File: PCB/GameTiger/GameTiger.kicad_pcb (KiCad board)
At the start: 2 copper layers, 86.4 x 107.2 mm, 73 parts, among them J1 USB_C_Receptacle_USB2.0, J2 503398-1892, J3 LCD Display, J4 Speaker, Q1 DMG3415, U1 RP2040, U2 MCP73831-2-OT, U3 W25Q128JVSIQ, U4 PAM8302A, U5 AP2112K-3.3, U6 PCF8574TS, Y1 ABLS-12MHZ-B4-T

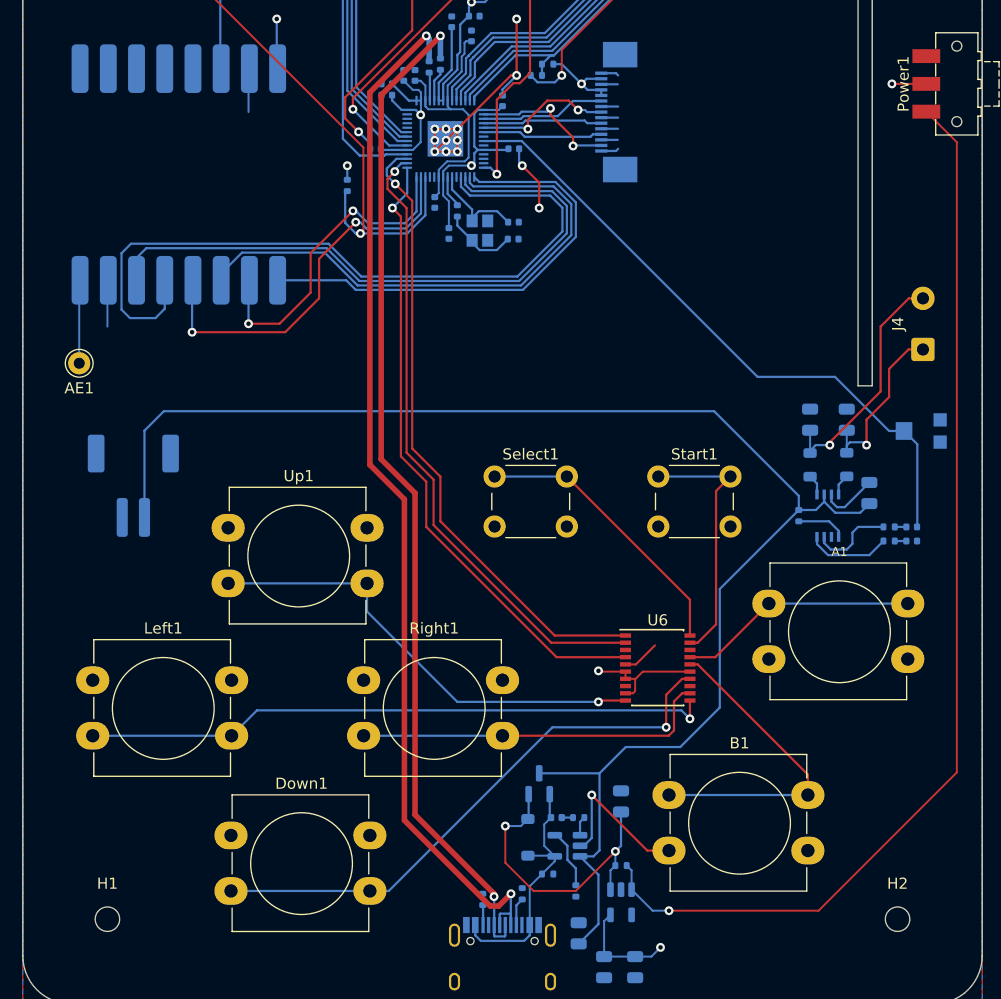
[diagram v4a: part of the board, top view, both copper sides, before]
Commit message: PCB layout and component reference completed
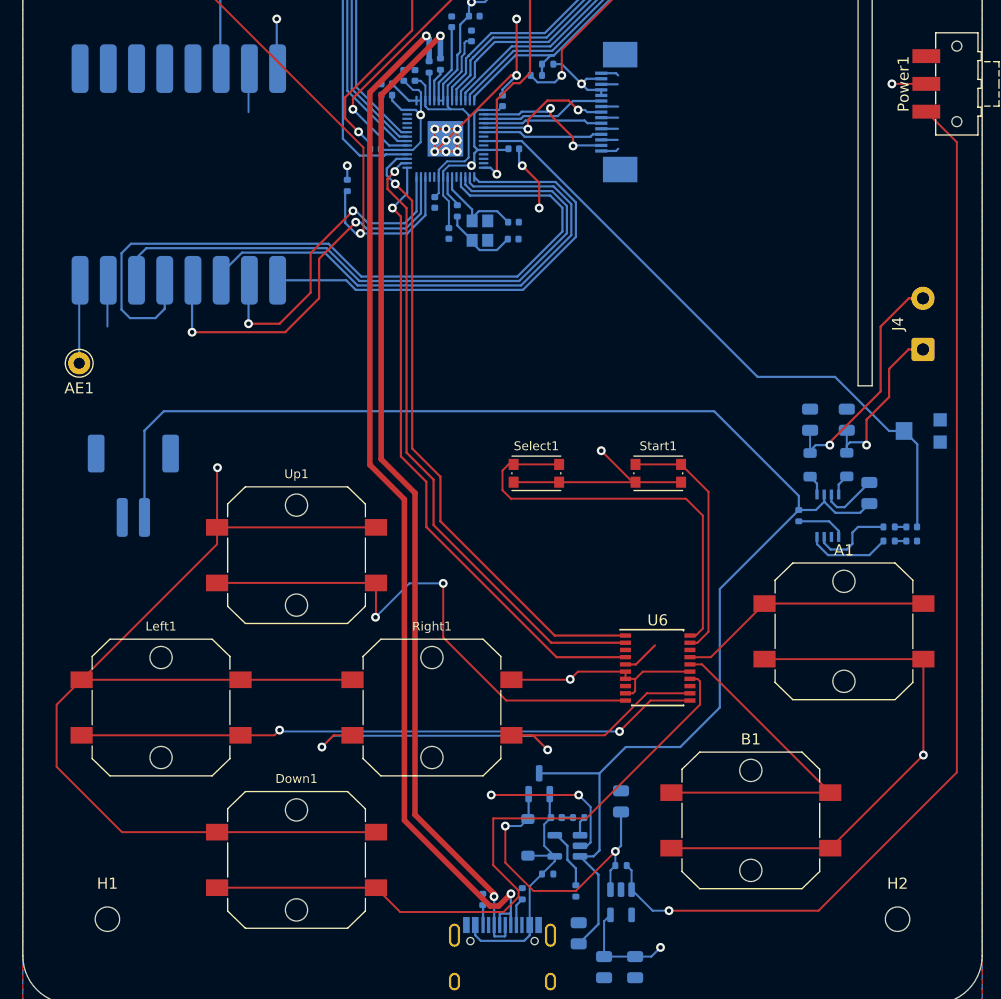
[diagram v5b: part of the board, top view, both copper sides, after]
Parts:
- A1, B1, Down1, Left1, Right1, Up1: footprint Button_Switch_THT:SW_PUSH-12mm_Wuerth-430476085716 -> Button_Switch_SMD:SW_Push_1P1T_NO_CK_PTS125Sx43PSMTR
- Select1, Start1: footprint Button_Switch_THT:SW_PUSH_6mm -> Button_Switch_SMD:SW_Push_1P1T_NO_CK_KMR2
- moved B1 7.71 mm to (98.6, 120.7)
- moved A1 7.21 mm to (106.9, 103.6)
- moved Up1 6.62 mm to (57.7, 96.8)
- moved Left1 6.62 mm to (45.5, 110.5)
- moved Right1 6.62 mm to (69.8, 110.5)
- moved Down1 6.30 mm to (57.7, 124.2)
- moved Select1 3.77 mm to (79.2, 89.4)
- moved Start1 0.29 mm to (90.2, 89.4)
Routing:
- net GND: track 153.3 -> 331.0 mm, vias 21 -> 25
- net KYBD_RIGHT: track 32.5 -> 45.9 mm, vias 0 -> 2
- net KYBD_SELECT: track 25.4 -> 37.7 mm
- net KYBD_DOWN: track 50.9 -> 62.6 mm, vias 1 -> 0
- net KYBD_UP: track 41.7 -> 48.4 mm, vias 1 -> 2
- net KYBD_B: track 29.1 -> 31.7 mm
- net SX1262_CS: track 57.2 -> 55.2 mm
- net KYBD_A: track 21.6 -> 23.0 mm
- net KYBD_START: track 23.4 -> 22.3 mm
- net SX1262_MISO: track 49.3 -> 48.6 mm
- net KYBD_LEFT: track 56.7 -> 56.2 mm, vias 1 -> 2

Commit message: Ready for uploading to JLCPCB
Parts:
- Power1: moved to B.Cu
- R1, R5: value 1kΩ -> 1k
- R10, R12, R13, R16, R6, R7: value 10KΩ -> 10K
- R11, R14, R15: value 5.1KΩ -> 5.1K
- R2: value 10kΩ -> 10K
- R3, R4: value 27Ω -> 27; footprint Resistor_SMD:R_0402_1005Metric -> Resistor_SMD:R_0603_1608Metric
- R8, R9: value 100Ω -> 100
- U6: footprint Package_SO:SSOP-20_4.4x6.5mm_P0.65mm -> PCF8574TS:SOP65P640X150-20N; moved to B.Cu
- moved AE1 29.2 mm to (38.1, 50.3)
- moved C15 6.72 mm to (72.4, 55.4)
- moved J2 5.79 mm to (74.7, 43.7), turned to -90 degrees
- moved Reset1 5.73 mm to (47.8, 38.1)
- moved Boot1 5.48 mm to (104.4, 38.1)
- moved C16 4.71 mm to (74.5, 52.9)
- moved C3 4.39 mm to (77.2, 72.7)
- moved Y1 4.39 mm to (74.2, 72.0)
- moved C8 4.39 mm to (77.2, 64.6)
- moved U3 4.39 mm to (91.4, 40.8)
- moved C12 4.39 mm to (65.8, 58.8)
- moved C13 4.39 mm to (70.1, 69.4)
- moved C14 4.39 mm to (76.2, 60.3)
- moved C2 4.39 mm to (77.2, 71.2)
- moved C5 4.39 mm to (65.8, 59.8)
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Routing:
- net GND: track 331.0 -> 276.0 mm, vias 25 -> 24
- net KYBD_UP: track 48.4 -> 79.0 mm, vias 2 -> 1
- net SX1262_DIO1: track 71.4 -> 49.4 mm
- net Net-(AE1-A): track 7.39 -> 28.7 mm
- net KYBD_A: track 23.0 -> 38.9 mm, vias 0 -> 1
- net MicroSD_CLK: track 29.0 -> 41.3 mm, vias 2 -> 0
- net MicroSD_DETECT: track 43.6 -> 52.8 mm
- net +3.3V: track 87.2 -> 79.7 mm, vias 8 -> 10
- net POWER_USB_DM: track 95.4 -> 88.7 mm
- net KYBD_SELECT: track 37.7 -> 31.3 mm, vias 0 -> 1
- net KYBD_LEFT: track 56.2 -> 50.3 mm, vias 2 -> 1
- net Net-(U1-RUN): track 57.9 -> 63.0 mm
- net MicroSD_MISO: track 38.5 -> 34.0 mm, vias 0 -> 2
- net KYBD_DOWN: track 62.6 -> 66.8 mm, vias 0 -> 1
- net POWER_USB_DP: track 91.5 -> 87.9 mm
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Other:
- board size 86.4 x 107.2 mm -> 86.4 x 99.8 mm

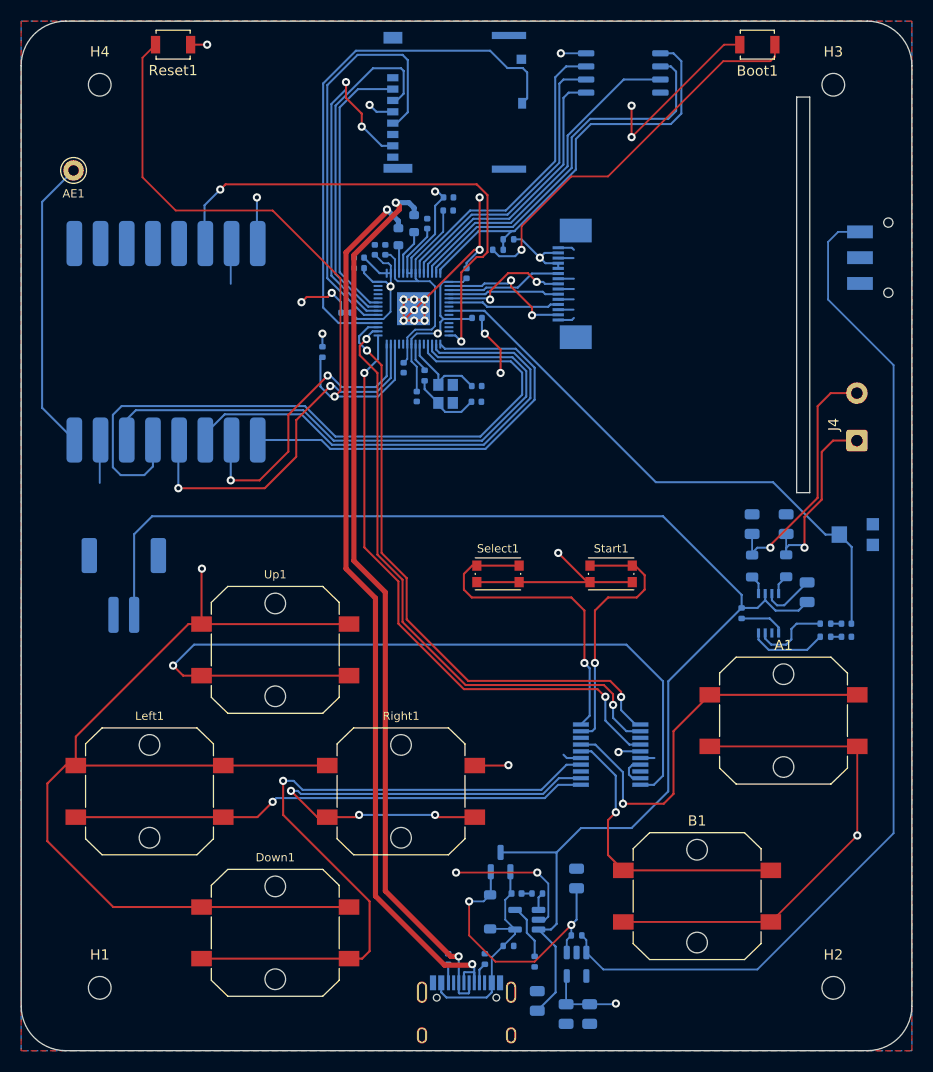
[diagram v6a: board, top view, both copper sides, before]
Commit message: Added battery level and charge detect connectors
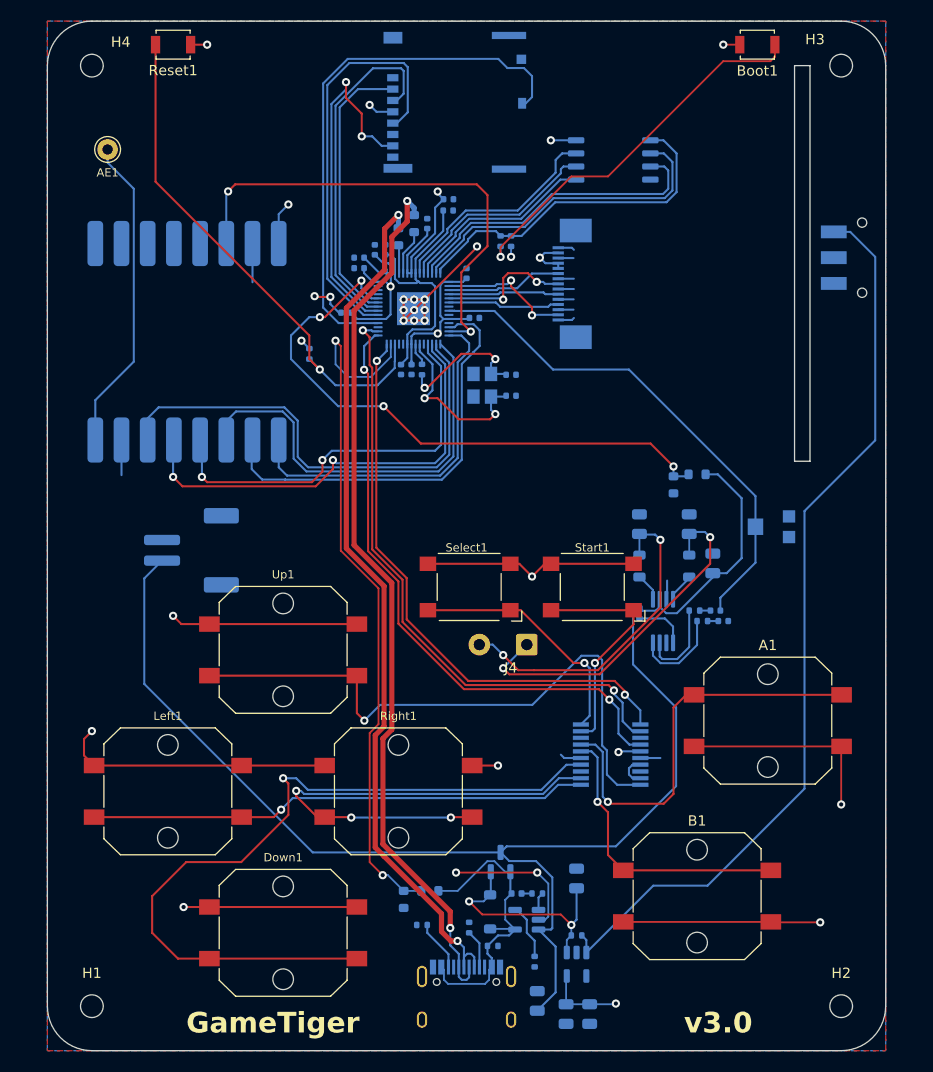
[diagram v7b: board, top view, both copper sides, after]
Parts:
- added R17: 100K, Resistor_SMD:R_0603_1608Metric, B.Cu at (98.6, 79.8)
- added R18: 100K, Resistor_SMD:R_0603_1608Metric, B.Cu at (96.3, 80.8)
- added R19: 5k6, Resistor_SMD:R_0603_1608Metric, B.Cu at (72.6, 120.1)
- added R20: 10K, Resistor_SMD:R_0603_1608Metric, B.Cu at (70.1, 121.0)
- C2, C3: value 27pF -> 30pF
- J1: value USB_C_Receptacle_USB2.0 -> USB TypeC Connector
- Select1, Start1: footprint Button_Switch_SMD:SW_Push_1P1T_NO_CK_KMR2 -> Button_Switch_SMD:SW_SPST_Omron_B3FS-105xP
- U4: footprint PAM8302A:PAM8302A -> Package_SO:MSOP-8_3x3mm_P0.65mm
- Y1: value ABLS-12MHZ-B4-T -> 12MHZ XTal; footprint Crystal:Crystal_SMD_2520-4Pin_2.5x2.0mm -> Crystal:Crystal_SMD_3225-4Pin_3.2x2.5mm
- moved J4 37.6 mm to (82.0, 96.3), turned to 180 degrees
- moved C17 12.8 mm to (100.3, 93.0)
- moved R8 12.8 mm to (98.3, 93.0)
- moved C18 12.0 mm to (101.1, 94.0)
- moved R9 12.0 mm to (99.1, 94.0)
- moved C21 10.9 mm to (93.0, 84.6)
- moved FB1 10.9 mm to (93.0, 88.6)
- moved U4 9.91 mm to (95.2, 94.0), turned to 90 degrees
- moved R6 9.91 mm to (93.0, 93.2)
- moved C22 9.56 mm to (100.1, 88.4)
- moved FB2 9.40 mm to (97.8, 88.6)
- moved C20 9.40 mm to (97.8, 84.6)
- moved U3 8.49 mm to (90.4, 49.3)
- moved R7 8.16 mm to (105.7, 84.8)
- moved X1 7.39 mm to (49.5, 87.1), turned to -90 degrees
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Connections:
- net POWER_USB_DM renamed POWER_USB_DN
- U1 pad 12: unconnected-(U1-GPIO9-Pad12) -> SX1262_RESET
- U1 pad 13: unconnected-(U1-GPIO10-Pad13) -> SX1262_DIO1
- U1 pad 14: SX1262_DIO1 -> SX1262_BUSY
- U1 pad 15: SX1262_BUSY -> SX1262_MISO
- U1 pad 16: SX1262_MISO -> SX1262_CS
- U1 pad 17: SX1262_CS -> SX1262_CLK
- U1 pad 18: SX1262_CLK -> SX1262_MOSI
- U1 pad 27: SX1262_MOSI -> POWER_DETECT
- U1 pad 28: SX1262_RESET -> KYBD_INT
- U1 pad 31: KYBD_INT -> unconnected-(U1-GPIO20-Pad31)
- U1 pad 38: unconnected-(U1-GPIO26_ADC0-Pad38) -> BATTERY_LVL
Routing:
- net GND: track 276.0 -> 188.6 mm, vias 24 -> 23
- net POWER_DETECT: track 0.00 -> 69.0 mm, vias 0 -> 2
- net BATTERY_LVL: track 0.00 -> 58.0 mm, vias 0 -> 4
- net SX1262_CLK: track 68.1 -> 43.5 mm, vias 0 -> 2
- net KYBD_UP: track 79.0 -> 59.7 mm
- net Net-(J4-Pin_1): track 18.5 -> 34.7 mm, vias 1 -> 2
- net Net-(U1-RUN): track 63.0 -> 50.4 mm
- net EN: track 101.2 -> 89.0 mm
- net SX1262_RESET: track 29.3 -> 40.9 mm, vias 2 -> 0
- net Crystal_XIN: track 8.60 -> 17.4 mm, vias 0 -> 2
- net Flash_QSPI_CLK: track 28.6 -> 20.1 mm
- net VBUS: track 21.8 -> 30.0 mm
- net Flash_QSPI_SD3: track 29.9 -> 21.6 mm
- net KYBD_DOWN: track 66.8 -> 75.0 mm
- net Net-(J4-Pin_2): track 24.0 -> 32.0 mm, vias 1 -> 2
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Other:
- board size 86.4 x 99.8 mm -> 81.3 x 99.8 mm
- board text added: "+"
- board text added: "-"
- board text added: "GameTiger"
- board text added: "v3.0"

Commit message: Completed updating the PCB design for peer review
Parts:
- removed R14, R15: 5.1K, Resistor_SMD:R_0402_1005Metric
- added R21: 5.1K, Resistor_SMD:R_0402_1005Metric, B.Cu at (72.4, 125.0)
- added R22: 5.1K, Resistor_SMD:R_0402_1005Metric, B.Cu at (76.5, 123.7)
- added REF**: OSHW-Logo2_14.6x12mm_Copper, Symbol:OSHW-Logo2_14.6x12mm_Copper, F.Cu at (43.9, 99.3)
- added REF**: OSHW-Logo2_14.6x12mm_Copper, Symbol:OSHW-Logo2_14.6x12mm_Copper, B.Cu at (101.9, 127.3)
- A1, B1, Down1, Left1, Right1, Up1: footprint Button_Switch_SMD:SW_Push_1P1T_NO_CK_PTS125Sx43PSMTR -> Button_Switch_THT:SW_PUSH-12mm
- AE1: footprint Connector_Pin:Pin_D1.0mm_L10.0mm -> Connector_Pin:Pin_D1.0mm_L10.0mm_LooseFit
- R17, R18, R19, R20, R3, R4: footprint Resistor_SMD:R_0603_1608Metric -> Resistor_SMD:R_0402_1005Metric
- Select1, Start1: footprint Button_Switch_SMD:SW_SPST_Omron_B3FS-105xP -> Button_Switch_THT:SW_TH_Tactile_Omron_B3F-10xx
- moved C3 13.4 mm to (68.1, 75.2), turned to 90 degrees
- moved Y1 7.85 mm to (70.9, 74.9), turned to 180 degrees
- moved A1 7.73 mm to (98.6, 100.1)
- moved C2 7.31 mm to (73.7, 74.7), turned to -90 degrees
- moved B1 7.07 mm to (95.4, 114.3)
- moved Down1 6.02 mm to (52.9, 121.7)
- moved Right1 5.83 mm to (64.1, 108.5)
- moved Up1 5.68 mm to (52.9, 95.3)
- moved Left1 5.59 mm to (42.0, 108.5)
- moved Select1 3.71 mm to (79.2, 93.2)
- moved Start1 3.19 mm to (90.3, 93.2)
- moved J4 2.84 mm to (79.2, 96.8), turned to 0 degrees
- moved AE1 1.27 mm to (40.1, 48.3)
- moved R3 0.97 mm to (70.9, 56.4)
- moved R4 0.43 mm to (69.6, 57.1)
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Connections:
- R18 pad 1: GND -> BATTERY_LVL
- R18 pad 2: BATTERY_LVL -> GND
- Y1 pad 1: Crystal_XOUT -> Crystal_XIN
- Y1 pad 2: Crystal_XIN -> GND
- Y1 pad 3: (no net) -> Crystal_XOUT
- Y1 pad 4: (no net) -> GND
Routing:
- net GND: track 188.6 -> 90.5 mm, vias 23 -> 19
- net KYBD_RIGHT: track 46.1 -> 24.9 mm, vias 3 -> 0
- net KYBD_DOWN: track 75.0 -> 57.7 mm
- net KYBD_UP: track 59.7 -> 46.5 mm, vias 1 -> 0
- net KYBD_A: track 39.5 -> 31.1 mm
- net KYBD_SELECT: track 23.8 -> 31.0 mm, vias 1 -> 2
- net Crystal_XOUT: track 12.9 -> 6.80 mm, vias 2 -> 0
- net Net-(J4-Pin_2): track 32.0 -> 26.4 mm, vias 2 -> 1
- net Crystal_XIN: track 17.4 -> 12.3 mm, vias 2 -> 0
- net SX1262_BUSY: track 34.9 -> 31.4 mm
- net KYBD_B: track 28.1 -> 24.6 mm
- net KYBD_START: track 22.5 -> 25.9 mm, vias 1 -> 2
- net SX1262_CS: track 48.0 -> 44.8 mm
- net SX1262_MISO: track 40.7 -> 37.7 mm
- net POWER_USB_DP: track 86.1 -> 89.1 mm
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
